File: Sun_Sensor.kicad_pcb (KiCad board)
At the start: 2 copper layers, 23.9 x 10 mm, 11 parts, among them J1 PicoBlade_01x03, J2 M2, J3 M2, U1 TSV7721IL

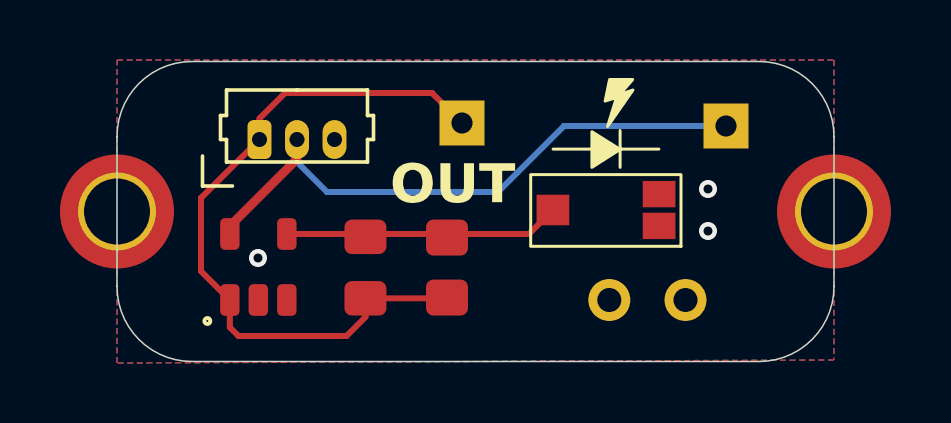
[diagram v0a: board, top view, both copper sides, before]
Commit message: minor reposition
Minor reposition of test-hook
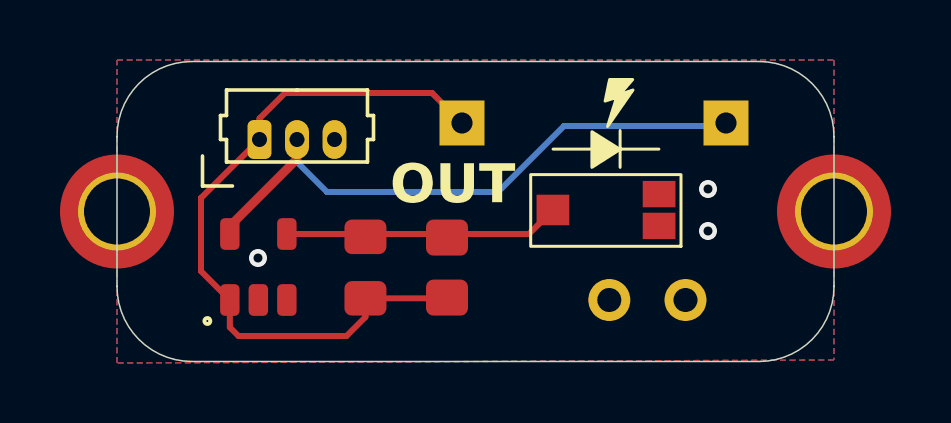
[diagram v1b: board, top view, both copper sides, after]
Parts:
- moved TP1 0.10 mm to (147.5, 55.0)
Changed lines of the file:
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@@
 	(footprint "TestPoint:TestPoint_THTPad_1.5x1.5mm_Drill0.7mm"
 		(layer "B.Cu")
-		(at 147.5 55.1 180)
+		(at 147.5 55 180)
 		(descr "THT rectangular pad as test Point, square 1.5mm side length, hole diameter 0.7mm")
 		(tags "test point THT pad rectangle square")
@@
 		(min_thickness 0.25)
 		(filled_areas_thickness no)
-		(fill yes
+		(fill
 			(thermal_gap 0.5)
 			(thermal_bridge_width 0.5)
